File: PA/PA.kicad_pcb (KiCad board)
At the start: 2 copper layers, 100 x 100 mm, 117 parts, among them J1 Conn_Coaxial, J10 Conn_01x01, J11 Conn_01x01, J12 Conn_01x01, J13 Conn_01x01, J14 Conn_01x01, J15 Conn_01x01, J16 Conn_01x01, J17 Conn_01x01, J18 Conn_01x01, J19 Conn_01x01, J2 Conn_01x02, J20 Conn_01x01, J21 Conn_01x01, J22 Conn_01x01, J23 Conn_01x01, J24 Conn_01x01, J25 Conn_01x01, J26 Conn_01x01, J3 Conn_Coaxial, J4 Conn_01x02, J5 Conn_01x02, J6 Conn_01x01, J7 Conn_01x01, J8 Conn_01x01, J9 Conn_01x01, Q1 2N3904, Q2 IRF510N, Q3 IRF510N, Q4 2N3906, Q5 IRF510N, Q6 2N3904, T1 Transformer_1P1Sdotted, T2 Transformer_1P1Sdotted, T3 Transformer_1P1Sdotted

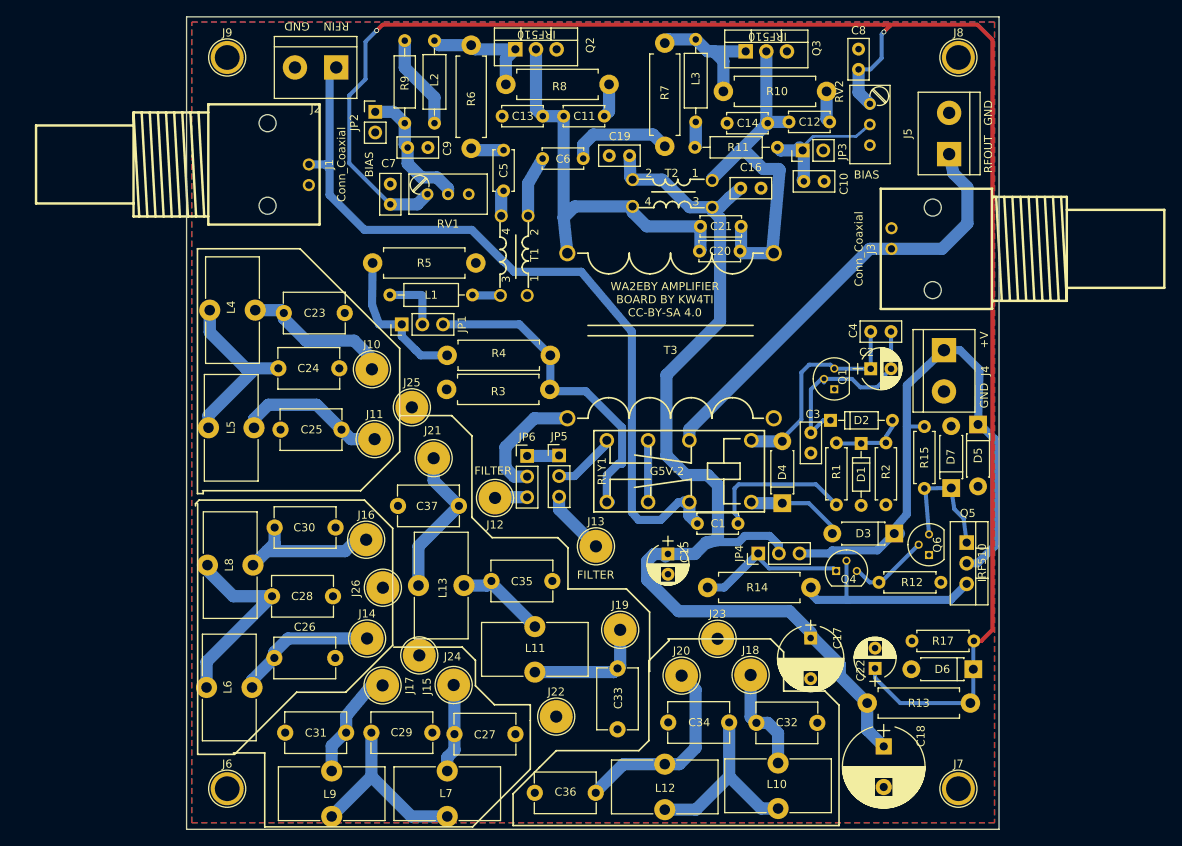
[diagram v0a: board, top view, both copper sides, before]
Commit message: Made filter capacitors mica or 1206 SMT
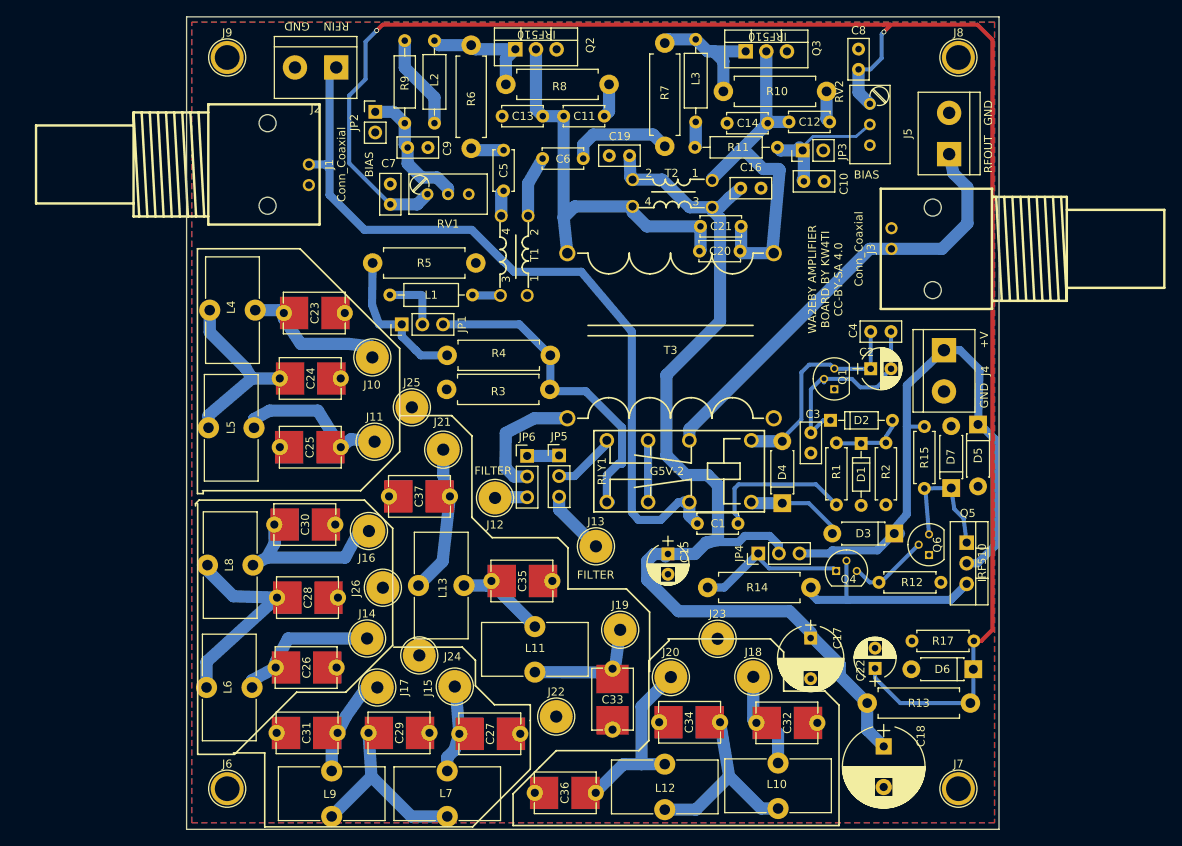
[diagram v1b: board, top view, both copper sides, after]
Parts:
- C23, C24, C25, C26, C27, C28, C29, C30, C31, C32, C33, C34, C35, C36, C37: footprint Capacitors_THT:C_Disc_D7.5mm_W5.0mm_P7.50mm -> PA:C_Disc_SMD
- moved C25 2.16 mm to (59.0, 93.0)
- moved C37 1.61 mm to (72.4, 99.0)
- moved J21 1.58 mm to (71.6, 93.3)
- moved J10 1.46 mm to (62.9, 81.9)
- moved J20 1.33 mm to (99.6, 121.3)
- moved C24 1.26 mm to (51.5, 84.5)
- moved C26 1.19 mm to (51.0, 120.1)
- moved J16 1.12 mm to (62.4, 103.3)
- moved C34 1.12 mm to (105.7, 126.8)
- moved C31 1.05 mm to (58.6, 128.1)
- moved J17 0.70 mm to (63.5, 122.5)
- moved C28 0.63 mm to (51.1, 111.5)
- moved C33 0.61 mm to (92.4, 120.2)
- moved C27 0.60 mm to (73.6, 128.2)
- moved J18 0.40 mm to (109.8, 121.2)
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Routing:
- net Net-(C30-Pad1): track 18.5 -> 20.8 mm
- net Net-(C36-Pad1): track 24.8 -> 22.7 mm
- net Net-(C28-Pad1): track 24.5 -> 25.4 mm
- net Net-(C31-Pad1): track 13.8 -> 12.9 mm
- net Net-(C37-Pad1): track 19.0 -> 18.1 mm
- net Net-(JP6-Pad2): track 14.7 -> 15.4 mm
- net Net-(C25-Pad1): track 18.4 -> 19.0 mm
- net Net-(C33-Pad1): track 15.2 -> 14.7 mm

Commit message: Add transmit disable switch
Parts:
- added C38: 100 nF, Capacitors_THT:C_Disc_D5.0mm_W2.5mm_P2.50mm, F.Cu at (130.8, 113.8)
- added C39: 1 nF, Capacitors_THT:C_Disc_D5.0mm_W2.5mm_P2.50mm, F.Cu at (130.3, 100.6)
- added D10: ZENER, Diodes_THT:D_DO-41_SOD81_P7.62mm_Horizontal, F.Cu at (83.8, 59.2)
- added D11: ZENER, Diodes_THT:D_DO-41_SOD81_P7.62mm_Horizontal, F.Cu at (118.4, 63.3)
- added D8: ZENER, Diodes_THT:D_DO-41_SOD81_P7.62mm_Horizontal, F.Cu at (84.1, 69.6)
- added D9: ZENER, Diodes_THT:D_DO-41_SOD81_P7.62mm_Horizontal, F.Cu at (114.9, 70.9)
- added J27: Conn_01x01, Connectors:1pin, F.Cu at (115.1, 86.7)
- added J28: Conn_01x01, Connectors:1pin, F.Cu at (114.9, 82.4)
- added R16: 470R, Resistors_THT:R_Axial_DIN0207_L6.3mm_D2.5mm_P7.62mm_Horizontal, F.Cu at (126.0, 86.9)
- moved Q1 3.53 mm to (121.0, 82.5), turned to 180 degrees
- moved Q2 2.45 mm to (82.9, 44.2)
- moved J1 2.29 mm to (40.4, 58.1)
- moved C6 2.09 mm to (83.8, 55.3)
- moved Q3 1.07 mm to (109.9, 44.2)
- moved T1 0.85 mm to (78.7, 69.3)
- moved C2 0.76 mm to (124.2, 82.5)
- moved C4 0.76 mm to (124.2, 78.0)
- moved C5 0.65 mm to (78.5, 56.7)
- moved C19 0.49 mm to (94.7, 56.6)
- moved C16 0.41 mm to (107.8, 61.1)
- moved RV1 0.38 mm to (69.3, 61.8)
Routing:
- net +28V: track 73.4 -> 89.1 mm
- net Net-(L2-Pad1): track 15.2 -> 19.7 mm
- net Net-(D11-Pad1): track 0.00 -> 3.50 mm
- net Net-(C2-Pad1): track 27.1 -> 30.5 mm
- net Net-(J27-Pad1): track 0.00 -> 3.35 mm
- net Net-(C6-Pad1): track 7.53 -> 10.7 mm
- net Net-(D10-Pad1): track 0.00 -> 2.90 mm
- net Net-(C11-Pad1): track 50.8 -> 53.4 mm
- net Net-(C12-Pad1): track 45.2 -> 47.5 mm
- net Net-(C1-Pad1): track 97.8 -> 100.1 mm
- net Net-(J3-Pad1): track 55.4 -> 57.5 mm
- net Net-(C6-Pad2): track 12.9 -> 11.5 mm
- net Net-(C39-Pad1): track 16.2 -> 15.1 mm
- net Net-(L3-Pad1): track 16.2 -> 17.1 mm
- net Net-(L1-Pad2): track 3.47 -> 2.62 mm
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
